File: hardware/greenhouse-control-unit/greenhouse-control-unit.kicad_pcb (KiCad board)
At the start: 4 copper layers, 150 x 90 mm, 53 parts, among them J1 Molex_KK-396_01x02, J10 Conn_ESP32_DevKitV1_Female, J11 Conn_01x05_Female, J12 Conn_01x05_Female, J13 Molex_KK-396_01x12, J14 Molex_KK-254_01x12, J2 Molex_KK-396_01x02, J3 Beep_Jumper, J4 Conn_01x01_Male, J5 Conn_01x01_Male, J6 Conn_01x01_Male, J7 Conn_01x01_Male, J8 Conn_01x09, J9 Conn_01x05_Female, Q1 BC547, Q2 BC547, Q3 BC337, Q4 BC547, Q5 2N3906, Q6 BC547, Q7 BC337, U1 PCF8574

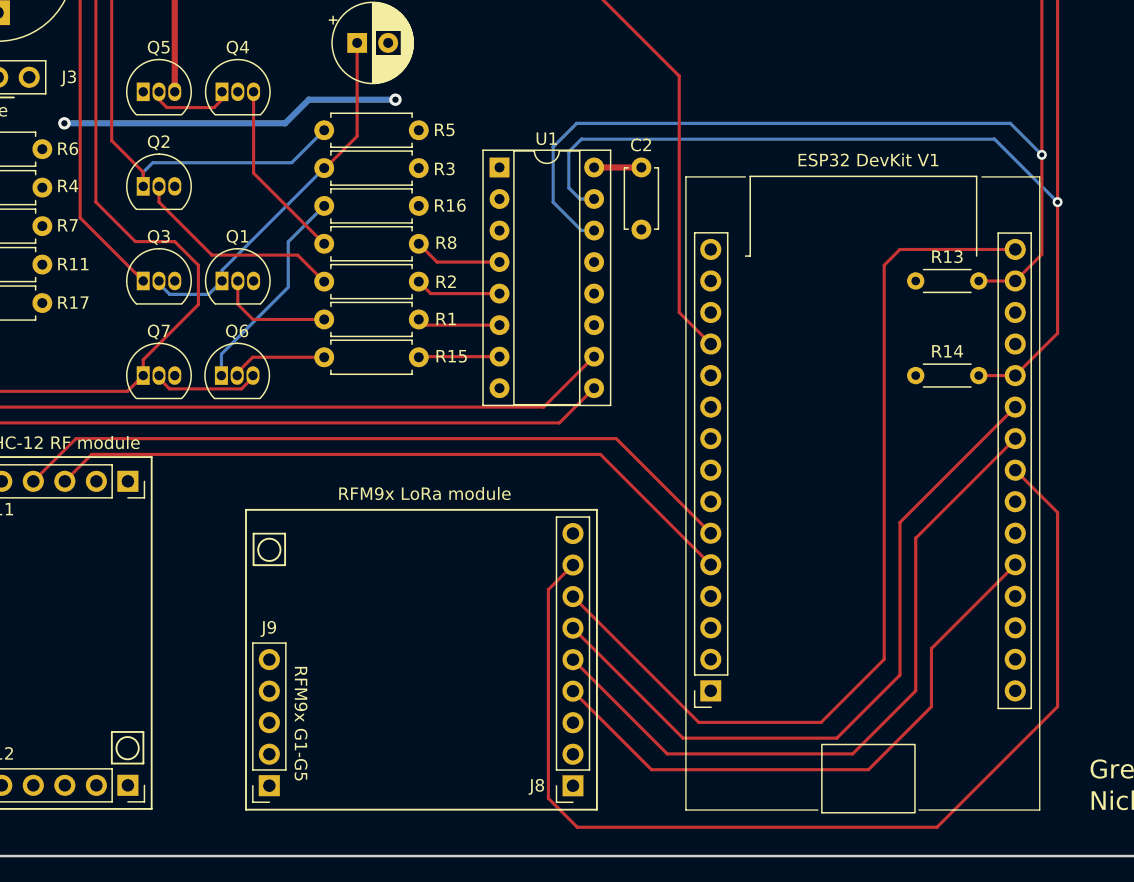
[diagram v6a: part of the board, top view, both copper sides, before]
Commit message: Use improved ESP32 footprint
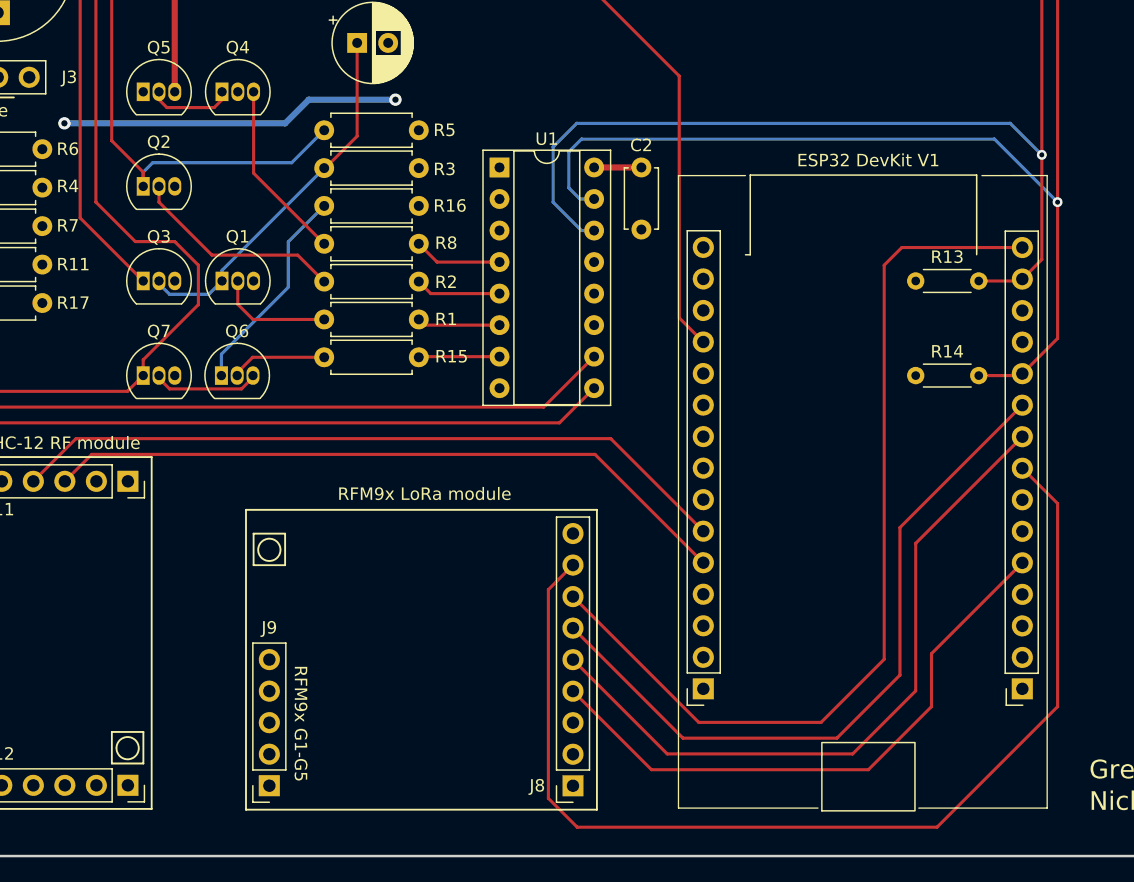
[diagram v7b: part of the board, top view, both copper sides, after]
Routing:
- net /HC12_RX: track 56.6 -> 55.9 mm
- net /HC12_TX: track 59.2 -> 58.5 mm
- net /MOSI: track 74.2 -> 74.8 mm

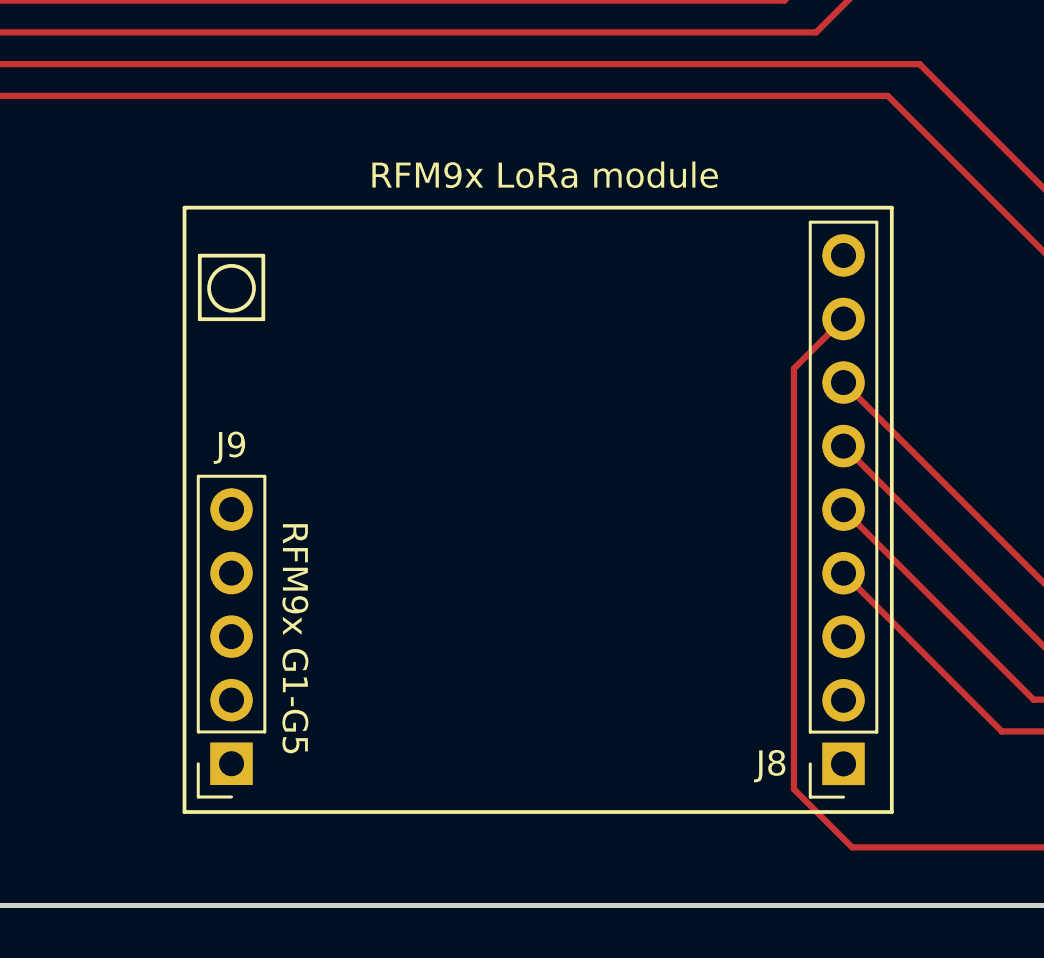
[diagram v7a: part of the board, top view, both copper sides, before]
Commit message: Widen RFM95 pin headers by 1mm
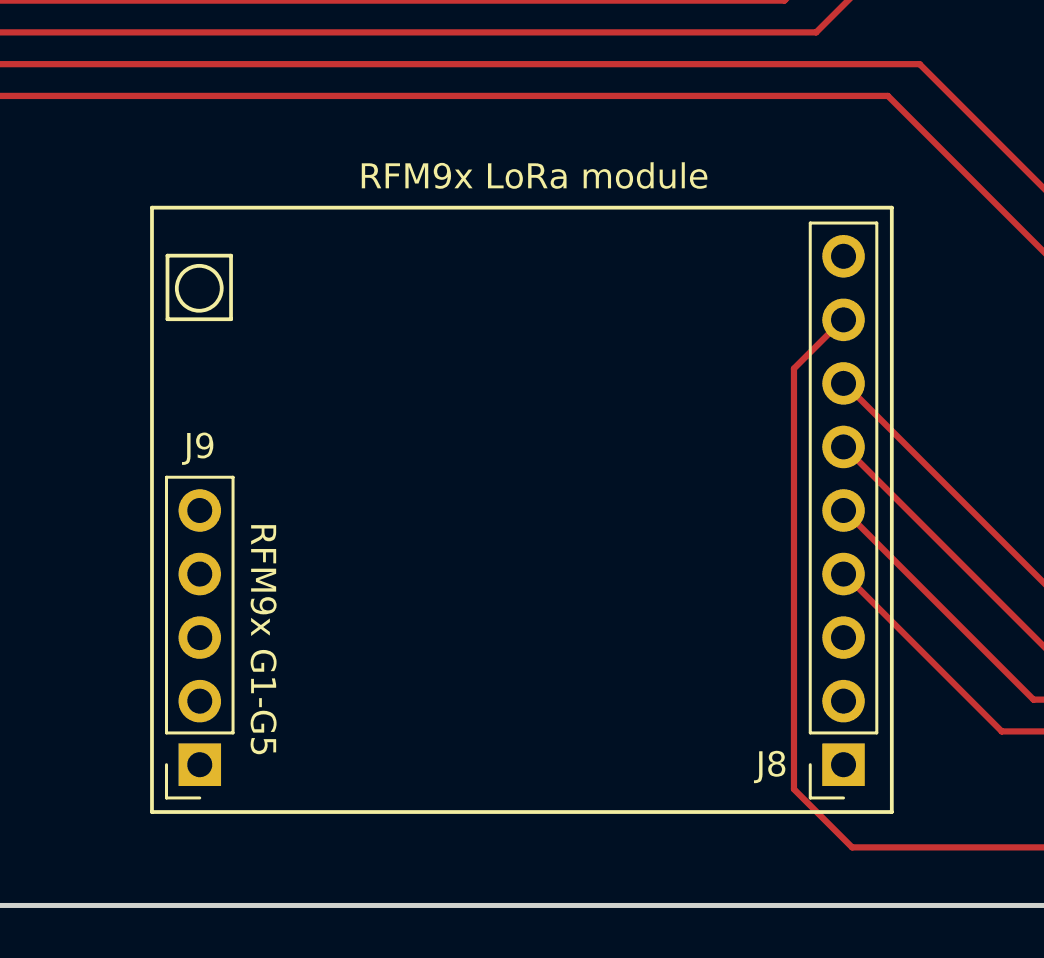
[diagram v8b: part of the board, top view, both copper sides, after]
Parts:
- moved J9 1.27 mm to (114.3, 128.8)
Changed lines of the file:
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@@
   )
   (footprint "Connector_PinSocket_2.54mm:PinSocket_1x09_P2.54mm_Vertical" (layer "F.Cu")
-    (at 140.0306 128.8038 180)
+    (at 140.0306 128.838 180)
     (descr "Through hole straight socket strip, 1x09, 2.54mm pitch, single row (from Kicad 4.0.7), script generated")
     (tags "Through hole socket strip THT 1x09 2.54mm single row")
@@
       (effects (font (size 1 1) (thickness 0.15)))
     )
-    (fp_text user "${Module}" (at 11.957217 23.495 unlocked) (layer "F.SilkS")
+    (fp_text user "${Module}" (at 12.3806 23.5 unlocked) (layer "F.SilkS")
       (effects (font (size 1 1) (thickness 0.15)))
     )
@@
   )
   (footprint "Connector_PinSocket_2.54mm:PinSocket_1x05_P2.54mm_Vertical" (layer "F.Cu")
-    (at 115.57 128.7988 180)
+    (at 114.3 128.838 180)
     (descr "Through hole straight socket strip, 1x05, 2.54mm pitch, single row (from Kicad 4.0.7), script generated")
     (tags "Through hole socket strip THT 1x05 2.54mm single row")
@@
     )
   )
-  (gr_circle (center 115.57 109.79685) (end 116.205 110.43185) (layer "F.SilkS") (width 0.15) (fill none))
+  (gr_circle (center 114.28 109.79685) (end 114.915 110.43185) (layer "F.SilkS") (width 0.15) (fill none))
   (gr_circle (center 104.1538 125.773425) (end 104.7888 126.408425) (layer "F.SilkS") (width 0.15) (fill none))
   (gr_line (start 198.247 62.103) (end 219.075 62.103) (layer "F.SilkS") (width 0.1))
@@
   (gr_rect (start 105.4238 127.009) (end 102.8838 124.469) (layer "F.SilkS") (width 0.15) (fill none))
   (gr_line (start 94.9926 73.3552) (end 89.811 73.3552) (layer "F.SilkS") (width 0.15))
-  (gr_rect (start 116.84 111.032425) (end 114.3 108.492425) (layer "F.SilkS") (width 0.15) (fill none))
+  (gr_rect (start 115.55 111.032425) (end 113.01 108.492425) (layer "F.SilkS") (width 0.15) (fill none))
   (gr_line (start 219.075 62.103) (end 219.075 105.918) (layer "F.SilkS") (width 0.1))
-  (gr_rect (start 141.9606 106.5738) (end 113.6904 130.7292) (layer "F.SilkS") (width 0.15) (fill none))
+  (gr_rect (start 141.9606 106.5738) (end 112.3904 130.7292) (layer "F.SilkS") (width 0.15) (fill none))
   (gr_rect (start 217.17 64.008) (end 200.17 104.008) (layer "Dwgs.User") (width 0.15) (fill none))
-  (gr_rect (start 140.0302 128.8496) (end 115.5556 108.4788) (layer "Dwgs.User") (width 0.15) (fill none))
+  (gr_rect (start 140.0302 128.8496) (end 114.2856 108.4788) (layer "Dwgs.User") (width 0.15) (fill none))
   (gr_rect (start 104.14 104.278) (end 94.017 128.778) (layer "Dwgs.User") (width 0.15) (fill none))
   (gr_rect locked (start 72.1356 44.4645) (end 222.1356 134.4645) (layer "Edge.Cuts") (width 0.2) (fill none))
